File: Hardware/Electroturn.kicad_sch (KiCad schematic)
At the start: 29 parts, among them J1 Encoder Terminal, J2 Stepper Motor Terminal, SW1 Feed Switch, SW2 Motor Braking Switch, SW3 Mode Right Scroll, SW4 Mode Left Scroll, SW5 Function Btn 1, SW6 Function Btn 2, SW7 Function Btn 2, SW8 Control Panel Encoder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

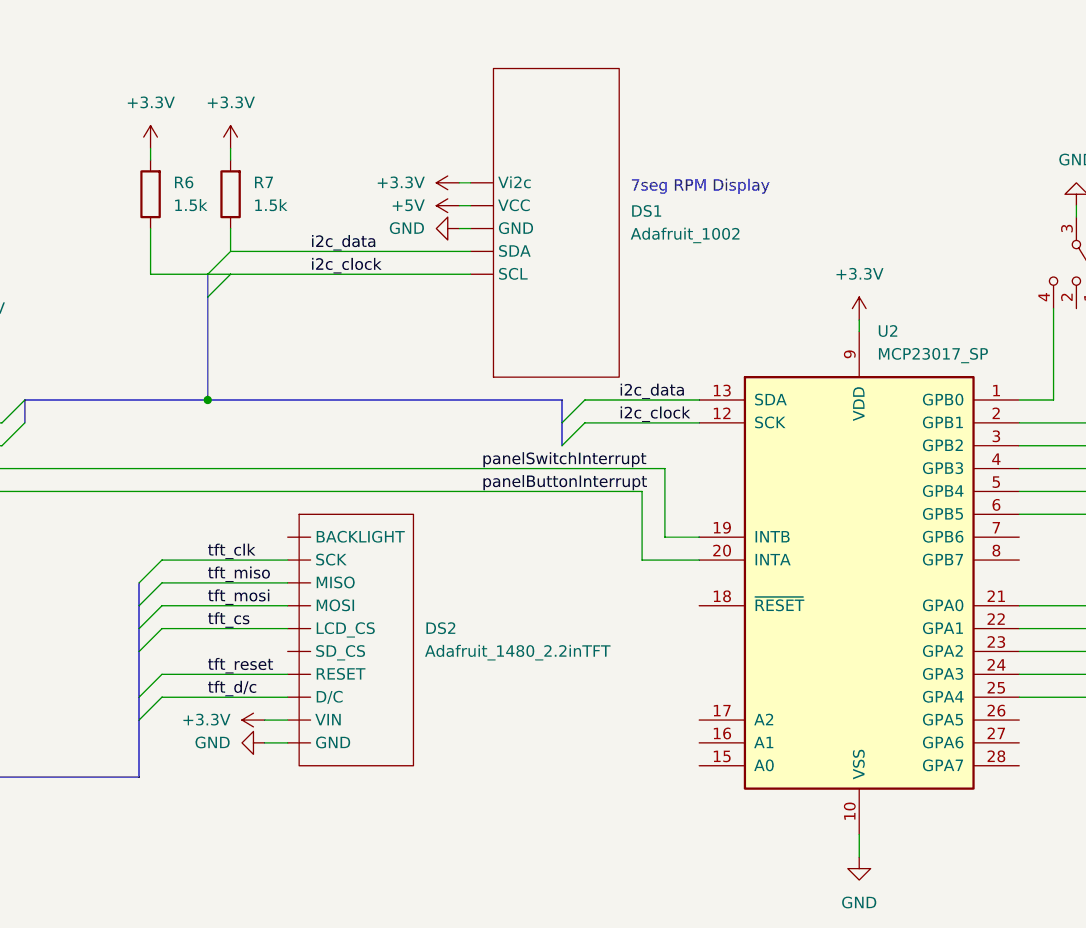
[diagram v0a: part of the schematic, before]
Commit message: Fixing broken symbol links from merge
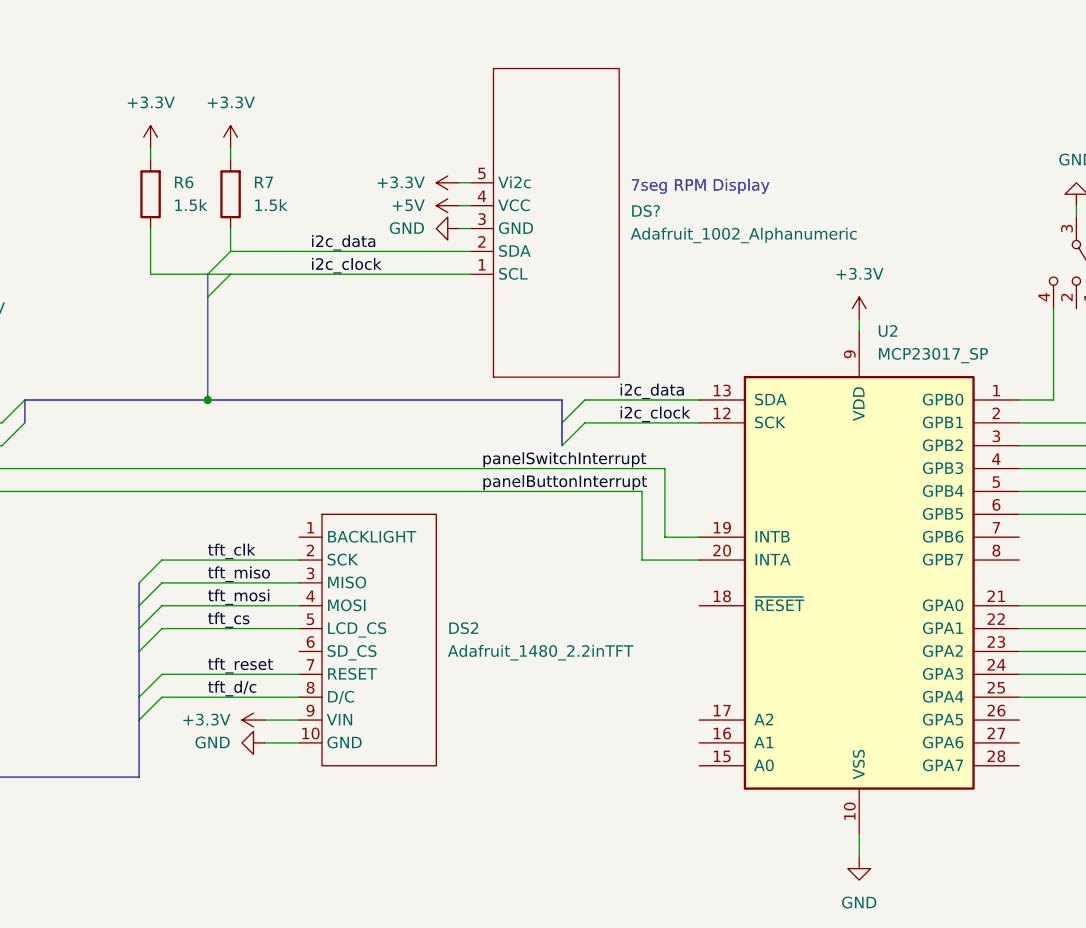
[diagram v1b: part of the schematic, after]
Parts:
- removed DS1: Adafruit_1002, symbol MCU_Module:Adafruit_1002
- added DS?: Adafruit_1002_Alphanumeric, symbol Electroturn_Parts:Adafruit_1002_Alphanumeric
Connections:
- net +3V3: now also DS2.9 (VIN), DS?.5 (Vi2c); no longer DS2. (VIN)
- net +5V: now also DS?.4 (VCC)
- net GND: now also DS2.10 (GND), DS?.3 (GND); no longer DS2. (VIN)
- net i2c_clock: now also DS?.1 (SCL)
- net i2c_data: now also DS?.2 (SDA)
- net tft_clk: now also DS2.2 (SCK); no longer DS2. (VIN)
- net tft_cs: now also DS2.5 (LCD_CS); no longer DS2. (VIN)
- net tft_d/c: now also DS2.8 (D/C); no longer DS2. (VIN)
- net tft_miso: now also DS2.3 (MISO); no longer DS2. (VIN)
- net tft_mosi: now also DS2.4 (MOSI); no longer DS2. (VIN)
- net tft_reset: now also DS2.7 (RESET); no longer DS2. (VIN)
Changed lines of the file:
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@@
+    (stroke (width 0) (type default) (color 0 0 0 0))
+  )
+  (wire (pts (xy 179.07 119.38) (xy 194.31 119.38))
     (stroke (width 0) (type default) (color 0 0 0 0))
   )
@@
     (stroke (width 0) (type default) (color 0 0 0 0))
   )
-  (wire (pts (xy 190.5 127) (xy 193.04 127))
+  (wire (pts (xy 190.5 127) (xy 194.31 127))
     (stroke (width 0) (type default) (color 0 0 0 0))
   )
@@
     (stroke (width 0) (type default) (color 0 0 0 0))
   )
-  (wire (pts (xy 179.07 114.3) (xy 193.04 114.3))
-    (stroke (width 0) (type default) (color 0 0 0 0))
-  )
   (wire (pts (xy 125.73 166.37) (xy 138.43 166.37))
     (stroke (width 0) (type default) (color 0 0 0 0))
@@
     (stroke (width 0) (type default) (color 0 0 0 0))
   )
-  (wire (pts (xy 179.07 109.22) (xy 193.04 109.22))
+  (wire (pts (xy 179.07 109.22) (xy 194.31 109.22))
     (stroke (width 0) (type default) (color 0 0 0 0))
   )
@@
     (stroke (width 0) (type default) (color 0 0 0 0))
   )
-  (wire (pts (xy 190.5 124.46) (xy 193.04 124.46))
+  (wire (pts (xy 190.5 124.46) (xy 194.31 124.46))
     (stroke (width 0) (type default) (color 0 0 0 0))
   )
@@
     (stroke (width 0) (type default) (color 0 0 0 0))
   )
+  (wire (pts (xy 179.07 114.3) (xy 194.31 114.3))
+    (stroke (width 0) (type default) (color 0 0 0 0))
+  )
   (bus (pts (xy 264.16 210.82) (xy 52.07 210.82))
     (stroke (width 0) (type default) (color 0 0 0 0))
@@
     (stroke (width 0) (type default) (color 0 0 0 0))
   )
-  (wire (pts (xy 179.07 121.92) (xy 193.04 121.92))
-    (stroke (width 0) (type default) (color 0 0 0 0))
-  )
   (wire (pts (xy 238.76 106.68) (xy 232.41 106.68))
     (stroke (width 0) (type default) (color 0 0 0 0))
@@
     (stroke (width 0) (type default) (color 0 0 0 0))
   )
+  (wire (pts (xy 179.07 121.92) (xy 194.31 121.92))
+    (stroke (width 0) (type default) (color 0 0 0 0))
+  )
   (bus (pts (xy 52.07 81.28) (xy 52.07 210.82))
     (stroke (width 0) (type default) (color 0 0 0 0))
   )
-  (wire (pts (xy 179.07 119.38) (xy 193.04 119.38))
-    (stroke (width 0) (type default) (color 0 0 0 0))
-  )
-  (wire (pts (xy 179.07 111.76) (xy 193.04 111.76))
+  (wire (pts (xy 179.07 111.76) (xy 194.31 111.76))
     (stroke (width 0) (type default) (color 0 0 0 0))
   )
@@
     (stroke (width 0) (type default) (color 0 0 0 0))
   )
-  (wire (pts (xy 179.07 106.68) (xy 193.04 106.68))
+  (wire (pts (xy 179.07 106.68) (xy 194.31 106.68))
     (stroke (width 0) (type default) (color 0 0 0 0))
   )
@@
     (pin "2")
   )
-  (symbol (lib_id "Electroturn_Parts:Adafruit_1480_2.2inTFT") (at 222.25 115.57 0) (unit 1)
-    (in_bom yes) (on_board yes) (fields_autoplaced)
-    (property "Reference" "DS2" (id 0) (at 208.28 114.2999 0)
-      (effects (font (size 1.27 1.27)) (justify left))
-    )
-    (property "Value" "Adafruit_1480_2.2inTFT" (id 1) (at 208.28 116.8399 0)
-      (effects (font (size 1.27 1.27)) (justify left))
-    )
-    (property "Footprint" "" (id 2) (at 208.28 134.62 0)
-      (effects (font (size 1.27 1.27)) hide)
-    )
-    (property "Datasheet" "" (id 3) (at 208.28 134.62 0)
-      (effects (font (size 1.27 1.27)) hide)
-    )
-    (pin "")
-    (pin "")
-    (pin "")
-    (pin "")
-    (pin "")
-    (pin "")
-    (pin "")
-    (pin "")
-    (pin "")
-    (pin "")
+  (symbol (lib_id "Electroturn_Parts:Adafruit_1480_2.2inTFT") (at 224.79 115.57 0) (unit 1)
+    (in_bom yes) (on_board yes) (fields_autoplaced)
+    (property "Reference" "DS2" (id 0) (at 210.82 114.2999 0)
+      (effects (font (size 1.27 1.27)) (justify left))
+    )
+    (property "Value" "Adafruit_1480_2.2inTFT" (id 1) (at 210.82 116.8399 0)
+      (effects (font (size 1.27 1.27)) (justify left))
+    )
+    (property "Footprint" "" (id 2) (at 210.82 134.62 0)
+      (effects (font (size 1.27 1.27)) hide)
+    )
+    (property "Datasheet" "" (id 3) (at 210.82 134.62 0)
+      (effects (font (size 1.27 1.27)) hide)
+    )
+    (pin "1")
+    (pin "10")
+    (pin "2")
+    (pin "3")
+    (pin "4")
+    (pin "5")
+    (pin "6")
+    (pin "7")
+    (pin "8")
+    (pin "9")
   )
   (symbol (lib_id "Device:R") (at 72.39 44.45 90) (unit 1)
@@
     (pin "1")
   )
+  (symbol (lib_id "Electroturn_Parts:Adafruit_1002_Alphanumeric") (at 223.52 69.85 90) (unit 1)
+    (in_bom yes) (on_board yes) (fields_autoplaced)
+    (property "Reference" "DS?" (id 0) (at 231.14 67.9449 90)
+      (effects (font (size 1.27 1.27)) (justify right))
+    )
+    (property "Value" "Adafruit_1002_Alphanumeric" (id 1) (at 231.14 70.4849 90)
+      (effects (font (size 1.27 1.27)) (justify right))
+    )
+    (property "Footprint" "" (id 2) (at 223.52 69.85 0)
+      (effects (font (size 1.27 1.27)) hide)
+    )
+    (property "Datasheet" "" (id 3) (at 223.52 69.85 0)
+      (effects (font (size 1.27 1.27)) hide)
+    )
+    (pin "1")
+    (pin "2")
+    (pin "3")
+    (pin "4")
+    (pin "5")
+  )
   (symbol (lib_id "power:GND") (at 85.09 71.12 180) (unit 1)
     (in_bom yes) (on_board yes) (fields_autoplaced)
@@
     (pin "1")
   )
-  (symbol (lib_id "MCU_Module:Adafruit_1002") (at 223.52 69.85 90) (unit 1)
-    (in_bom yes) (on_board yes) (fields_autoplaced)
-    (property "Reference" "DS1" (id 0) (at 231.14 67.9449 90)
-      (effects (font (size 1.27 1.27)) (justify right))
-    )
-    (property "Value" "Adafruit_1002" (id 1) (at 231.14 70.4849 90)
-      (effects (font (size 1.27 1.27)) (justify right))
-    )
-    (property "Footprint" "" (id 2) (at 223.52 69.85 0)
-      (effects (font (size 1.27 1.27)) hide)
-    )
-    (property "Datasheet" "" (id 3) (at 223.52 69.85 0)
-      (effects (font (size 1.27 1.27)) hide)
-    )
-    (pin "")
-    (pin "")
-    (pin "")
-    (pin "")
-    (pin "")
-  )
   (symbol (lib_id "power:GND") (at 285.75 175.26 180) (unit 1)
     (in_bom yes) (on_board yes) (fields_autoplaced)
@@
       (reference "D1") (unit 1) (value "Spindle Overspeed LED") (footprint "")
     )
-    (path "/fad358eb-4b7a-4138-896b-0d1749221b0d"
-      (reference "DS1") (unit 1) (value "Adafruit_1002") (footprint "")
-    )
     (path "/576ae6c6-a44d-4f6f-b20f-bbfc48447eb6"
       (reference "DS2") (unit 1) (value "Adafruit_1480_2.2inTFT") (footprint "")
     )
+    (path "/a072b0ff-1f7a-45c3-af75-d1bbb7cec40b"
+      (reference "DS?") (unit 1) (value "Adafruit_1002_Alphanumeric") (footprint "")
+    )
     (path "/8314209d-97cb-4c91-a11c-c6feda840b33"

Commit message: Quick fixes: schematic housekeeping
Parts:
- SW1: symbol Switch:SW_DP3T -> Switch:SW_SPDT_MSM
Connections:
- net +3V3: now also U2.18 (~{RESET})
- net GND: now also SW1.2, U2.15 (A0), U2.16 (A1), U2.17 (A2); no longer SW1.3
- net at U2.1 (GPB0): now also SW1.3; no longer SW1.4
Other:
- note added: "Address Setting Pins"
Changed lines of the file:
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@@
   (junction (at 311.15 186.69) (diameter 0) (color 0 0 0 0)
   )
+  (junction (at 237.49 129.54) (diameter 0) (color 0 0 0 0)
+  )
   (junction (at 184.15 88.9) (diameter 0) (color 0 0 0 0)
   )
@@
   (junction (at 311.15 191.77) (diameter 0) (color 0 0 0 0)
   )
+  (junction (at 237.49 127) (diameter 0) (color 0 0 0 0)
+  )
   (junction (at 118.11 158.75) (diameter 0) (color 0 0 0 0)
   )
@@
     (stroke (width 0) (type default) (color 0 0 0 0))
   )
+  (wire (pts (xy 237.49 127) (xy 237.49 129.54))
+    (stroke (width 0) (type default) (color 0 0 0 0))
+  )
   (wire (pts (xy 86.36 166.37) (xy 83.82 166.37))
     (stroke (width 0) (type default) (color 0 0 0 0))
@@
     (stroke (width 0) (type default) (color 0 0 0 0))
   )
+  (wire (pts (xy 237.49 127) (xy 238.76 127))
+    (stroke (width 0) (type default) (color 0 0 0 0))
+  )
   (wire (pts (xy 83.82 166.37) (xy 83.82 163.83))
     (stroke (width 0) (type default) (color 0 0 0 0))
@@
     (stroke (width 0) (type default) (color 0 0 0 0))
   )
+  (wire (pts (xy 238.76 124.46) (xy 237.49 124.46))
+    (stroke (width 0) (type default) (color 0 0 0 0))
+  )
   (bus (pts (xy 223.52 88.9) (xy 223.52 91.44))
     (stroke (width 0) (type default) (color 0 0 0 0))
@@
     (stroke (width 0) (type default) (color 0 0 0 0))
   )
+  (wire (pts (xy 237.49 129.54) (xy 238.76 129.54))
+    (stroke (width 0) (type default) (color 0 0 0 0))
+  )
   (wire (pts (xy 91.44 44.45) (xy 111.76 44.45))
     (stroke (width 0) (type default) (color 0 0 0 0))
@@
     (stroke (width 0) (type default) (color 0 0 0 0))
   )
+  (wire (pts (xy 237.49 124.46) (xy 237.49 127))
+    (stroke (width 0) (type default) (color 0 0 0 0))
+  )
   (wire (pts (xy 66.04 181.61) (xy 86.36 181.61))
     (stroke (width 0) (type default) (color 0 0 0 0))
@@
     (stroke (width 0) (type default) (color 0 0 0 0))
   )
+  (wire (pts (xy 237.49 129.54) (xy 237.49 130.81))
+    (stroke (width 0) (type default) (color 0 0 0 0))
+  )
   (wire (pts (xy 66.04 86.36) (xy 87.63 86.36))
     (stroke (width 0) (type default) (color 0 0 0 0))
   )
+  (wire (pts (xy 237.49 111.76) (xy 238.76 111.76))
+    (stroke (width 0) (type default) (color 0 0 0 0))
+  )
   (wire (pts (xy 179.07 114.3) (xy 194.31 114.3))
     (stroke (width 0) (type default) (color 0 0 0 0))
@@
   )
   (text "7seg RPM Display" (at 231.14 66.04 0)
+    (effects (font (size 1.27 1.27)) (justify left bottom))
+  )
+  (text "Address\nSetting\nPins" (at 228.6 129.54 0)
     (effects (font (size 1.27 1.27)) (justify left bottom))
   )
@@
     (pin "1")
     (pin "2")
+  )
+  (symbol (lib_id "power:GND") (at 237.49 130.81 0) (unit 1)
+    (in_bom yes) (on_board yes) (fields_autoplaced)
+    (property "Reference" "#PWR?" (id 0) (at 237.49 137.16 0)
+      (effects (font (size 1.27 1.27)) hide)
+    )
+    (property "Value" "GND" (id 1) (at 237.49 135.89 0))
+    (property "Footprint" "" (id 2) (at 237.49 130.81 0)
+      (effects (font (size 1.27 1.27)) hide)
+    )
+    (property "Datasheet" "" (id 3) (at 237.49 130.81 0)
+      (effects (font (size 1.27 1.27)) hide)
+    )
+    (pin "1")
   )
   (symbol (lib_id "Device:R") (at 87.63 58.42 90) (unit 1)
@@
     (pin "1")
   )
-  (symbol (lib_id "Switch:SW_DP3T") (at 280.67 73.66 270) (unit 1)
+  (symbol (lib_id "Switch:SW_SPDT_MSM") (at 280.67 73.66 270) (unit 1)
     (in_bom yes) (on_board yes) (fields_autoplaced)
     (property "Reference" "SW1" (id 0) (at 284.48 72.3899 90)
@@
       (effects (font (size 1.27 1.27)) (justify left))
     )
-    (property "Footprint" "" (id 2) (at 285.115 57.785 0)
-      (effects (font (size 1.27 1.27)) hide)
-    )
-    (property "Datasheet" "~" (id 3) (at 285.115 57.785 0)
+    (property "Footprint" "" (id 2) (at 280.67 73.66 0)
+      (effects (font (size 1.27 1.27)) hide)
+    )
+    (property "Datasheet" "~" (id 3) (at 280.67 73.66 0)
       (effects (font (size 1.27 1.27)) hide)
     )
@@
     (pin "2")
     (pin "3")
-    (pin "4")
   )
   (symbol (lib_id "power:GND") (at 66.04 45.72 0) (unit 1)
@@
     (pin "2")
   )
+  (symbol (lib_id "power:+3.3V") (at 237.49 111.76 90) (unit 1)
+    (in_bom yes) (on_board yes) (fields_autoplaced)
+    (property "Reference" "#PWR?" (id 0) (at 241.3 111.76 0)
+      (effects (font (size 1.27 1.27)) hide)
+    )
+    (property "Value" "+3.3V" (id 1) (at 233.68 111.7599 90)
+      (effects (font (size 1.27 1.27)) (justify left))
+    )
+    (property "Footprint" "" (id 2) (at 237.49 111.76 0)
+      (effects (font (size 1.27 1.27)) hide)
+    )
+    (property "Datasheet" "" (id 3) (at 237.49 111.76 0)
+      (effects (font (size 1.27 1.27)) hide)
+    )
+    (pin "1")
+  )
   (symbol (lib_id "Device:R") (at 177.8 66.04 180) (unit 1)
     (in_bom yes) (on_board yes) (fields_autoplaced)
@@
       (reference "#PWR?") (unit 1) (value "GND") (footprint "")
     )
+    (path "/3cad4c2c-33dc-4254-8b48-6c0b86892a68"
+      (reference "#PWR?") (unit 1) (value "GND") (footprint "")
+    )
     (path "/6f6dcca1-c45b-4c54-9099-c3854646d290"
       (reference "#PWR?") (unit 1) (value "GND") (footprint "")
@@
       (reference "#PWR?") (unit 1) (value "+3.3V") (footprint "")
     )
+    (path "/ca7b197f-7808-47de-a461-95f69fe0e8ed"
+      (reference "#PWR?") (unit 1) (value "+3.3V") (footprint "")
+    )

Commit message: Initial PCB work
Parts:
- C1, C2: renamed from C?; footprint (none) -> Capacitor_THT:C_Disc_D9.0mm_W5.0mm_P7.50mm
- D1: footprint (none) -> LED_THT:LED_D5.0mm
- DS1: renamed from DS?; footprint (none) -> Electroturn_Parts:Adafruit1002_0.54inAlphanumericBackpack
- DS2: footprint (none) -> Electroturn_Parts:Adafruit1480_TFTwithHeaders
- R10, R11, R8, R9: renamed from R?; footprint (none) -> Resistor_THT:R_Axial_DIN0411_L9.9mm_D3.6mm_P12.70mm_Horizontal
- R6, R7: footprint (none) -> Resistor_THT:R_Axial_DIN0411_L9.9mm_D3.6mm_P12.70mm_Horizontal
- SW1: footprint (none) -> Electroturn_Parts:SPDT_OnOffOn_ToggleSwitch_fromECEdepartment_CircularPads
- SW2: footprint (none) -> Electroturn_Parts:SW_SPDT_CK_ A11405RNZQ
- SW3, SW4, SW5, SW6, SW7: footprint (none) -> Button_Switch_THT:SW_PUSH_6mm
- SW8: footprint (none) -> Electroturn_Parts:CUIDevices_ACZ11BR1E20FD112C
- renumbered R5 to R3, R3 to R4, R4 to R5
